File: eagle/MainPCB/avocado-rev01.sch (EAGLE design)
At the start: 163 parts, among them IC2 3V#, IC5 3V#, IC6 MCP73811/2, J1 10118194-0001LF, J2 CONNECTOR-10HEADER-5X2, J3 0475710001, J4 CONNECTOR-4HEADER4, J5 CONNECTOR-3HEADER3, J6 HR911105A, P2 CONNECTOR-15686115148922, U1 V3S, U2 AP65111A, U3 AP65111A, U4 AP65111A, U5 PMIC-LDO-XC6206P302MR(SOT23)

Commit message: in progress
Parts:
- removed C43: 10u, marius:C0603
- removed CLK, INT, RST, WOL: TEST_TESTPOINT, marius:TEST_TESTPOINT
- removed J2: CONNECTOR-10HEADER-5X2, marius:CONNECTOR-10HEADER-5X2
- added DIGITAL1, DIGITAL2, DIGITAL3, PB2, PB3: TEST_TESTPOINT, marius:TEST_TESTPOINT
- added SW1, SW2, SW3: SPST_TACT-KMR2, adafruit:SPST_TACT-KMR2
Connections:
- removed net CLK: CLK.2, J2.10
- removed net INT: INT.2, J2.9
- removed net RST: J2.3, RST.2
- removed net WOL: J2.8, WOL.2
- new net N$54: PB2.2, SW2.P, U1G$2.PB2
- new net N$57: PB3.2, U1G$2.PB3
- new net N$58: DIGITAL1.2, SW3.P, U1G$2.PG3/SDC1/D1
- new net N$61: DIGITAL2.2, SW1.P, U1G$2.PG4/SDC1/D2
- new net N$62: DIGITAL3.2, U1G$2.PG5/SDC1/D3
- net 3V3: no longer C43.1, J2.2
- net CS: no longer J2.4
- net GND: now also SW1.S, SW2.S, SW3.S; no longer C43.2, J2.1
- net MISO: no longer J2.7
- net MOSI: no longer J2.6
- net SCK: no longer J2.5

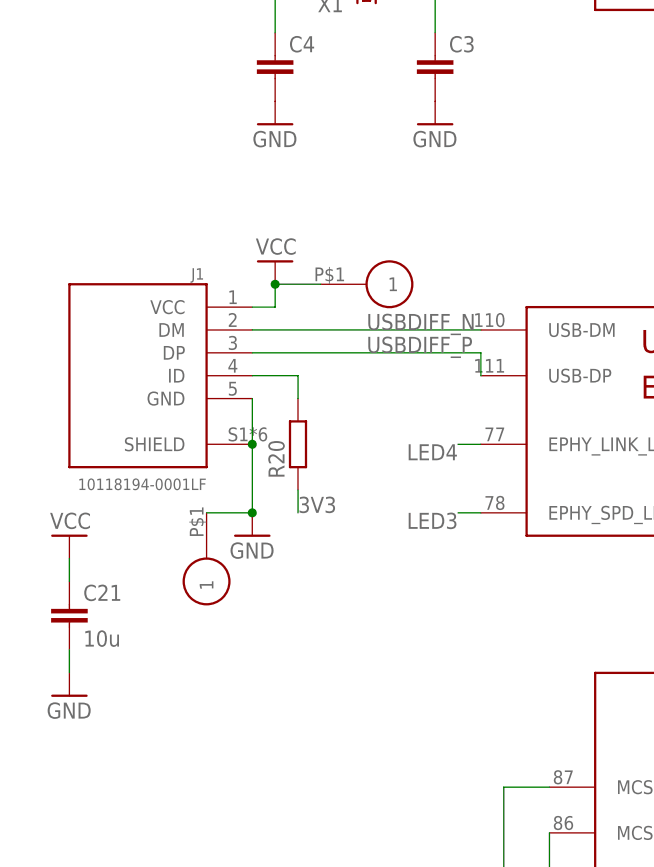
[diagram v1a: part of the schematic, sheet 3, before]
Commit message: Changed usb connector
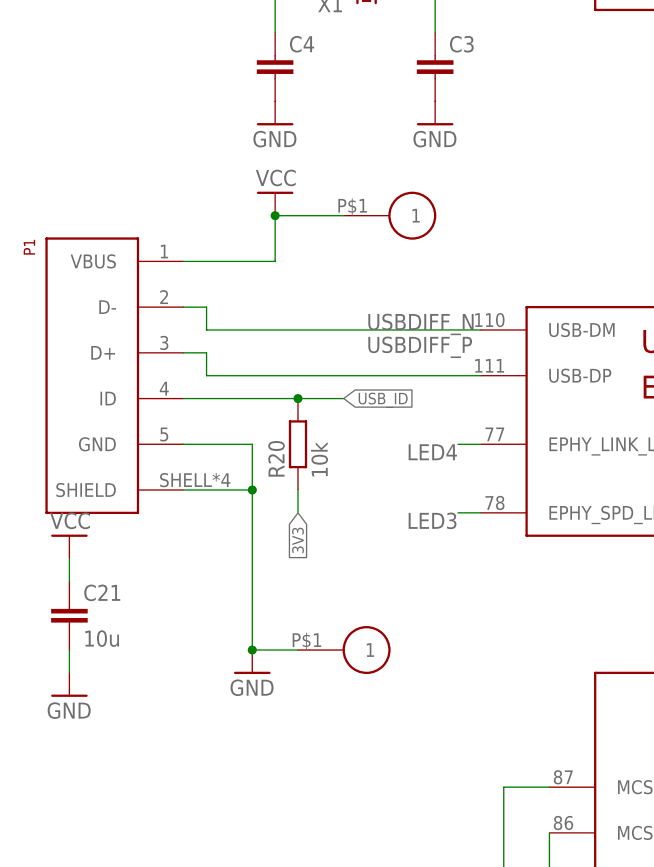
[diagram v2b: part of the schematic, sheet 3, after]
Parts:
- removed J1: 10118194-0001LF, 10118194-0001LF:10118194-0001LF
- added P1: USB629105150521, marius:USB629105150521
- R20: value (none) -> 10k
- R21, R22, R23, R24, R25, R26: device resistor:R-EU_R0402 -> marius:R0402
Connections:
- removed net USB-ID: J1.ID, R20.2
- new net USB_ID: P1.ID, R20.2, U1G$2.PF6
- net GND: now also P1.GND, P1.SHIELD; no longer J1.GND, J1.SHIELD
- net USBDIFF_N: now also P1.D-; no longer J1.DM
- net USBDIFF_P: now also P1.D+; no longer J1.DP
- net VCC: now also P1.VBUS; no longer J1.VCC

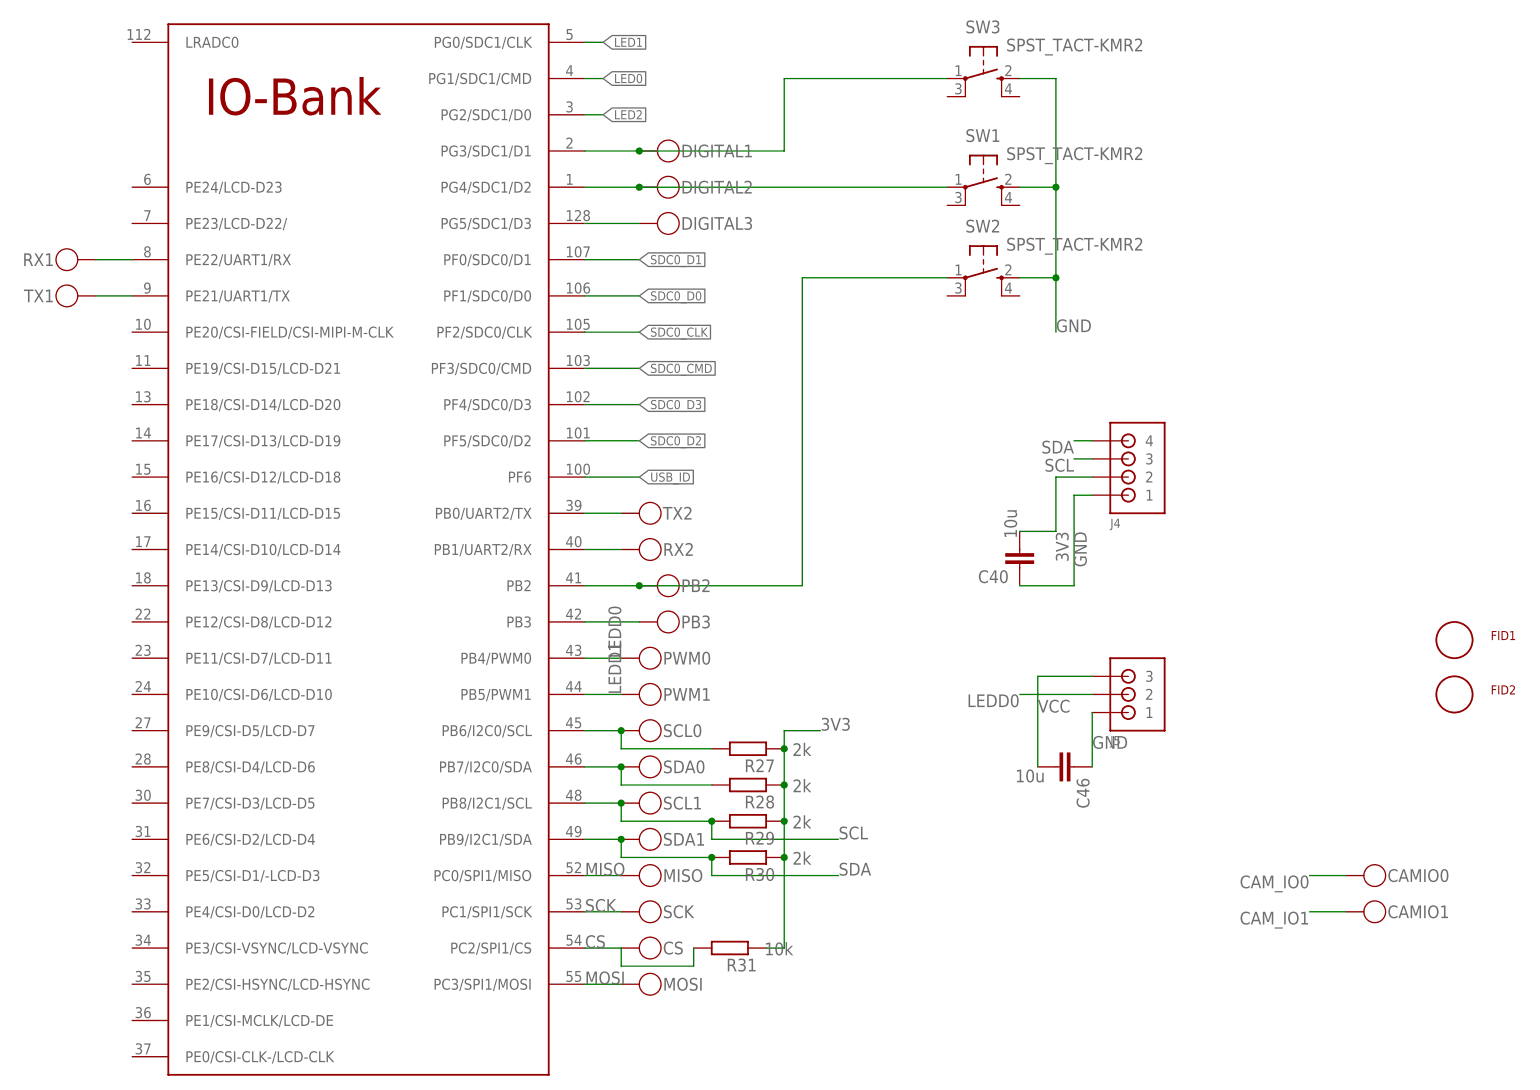
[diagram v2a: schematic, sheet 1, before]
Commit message: Added pin header for RX0/TX0
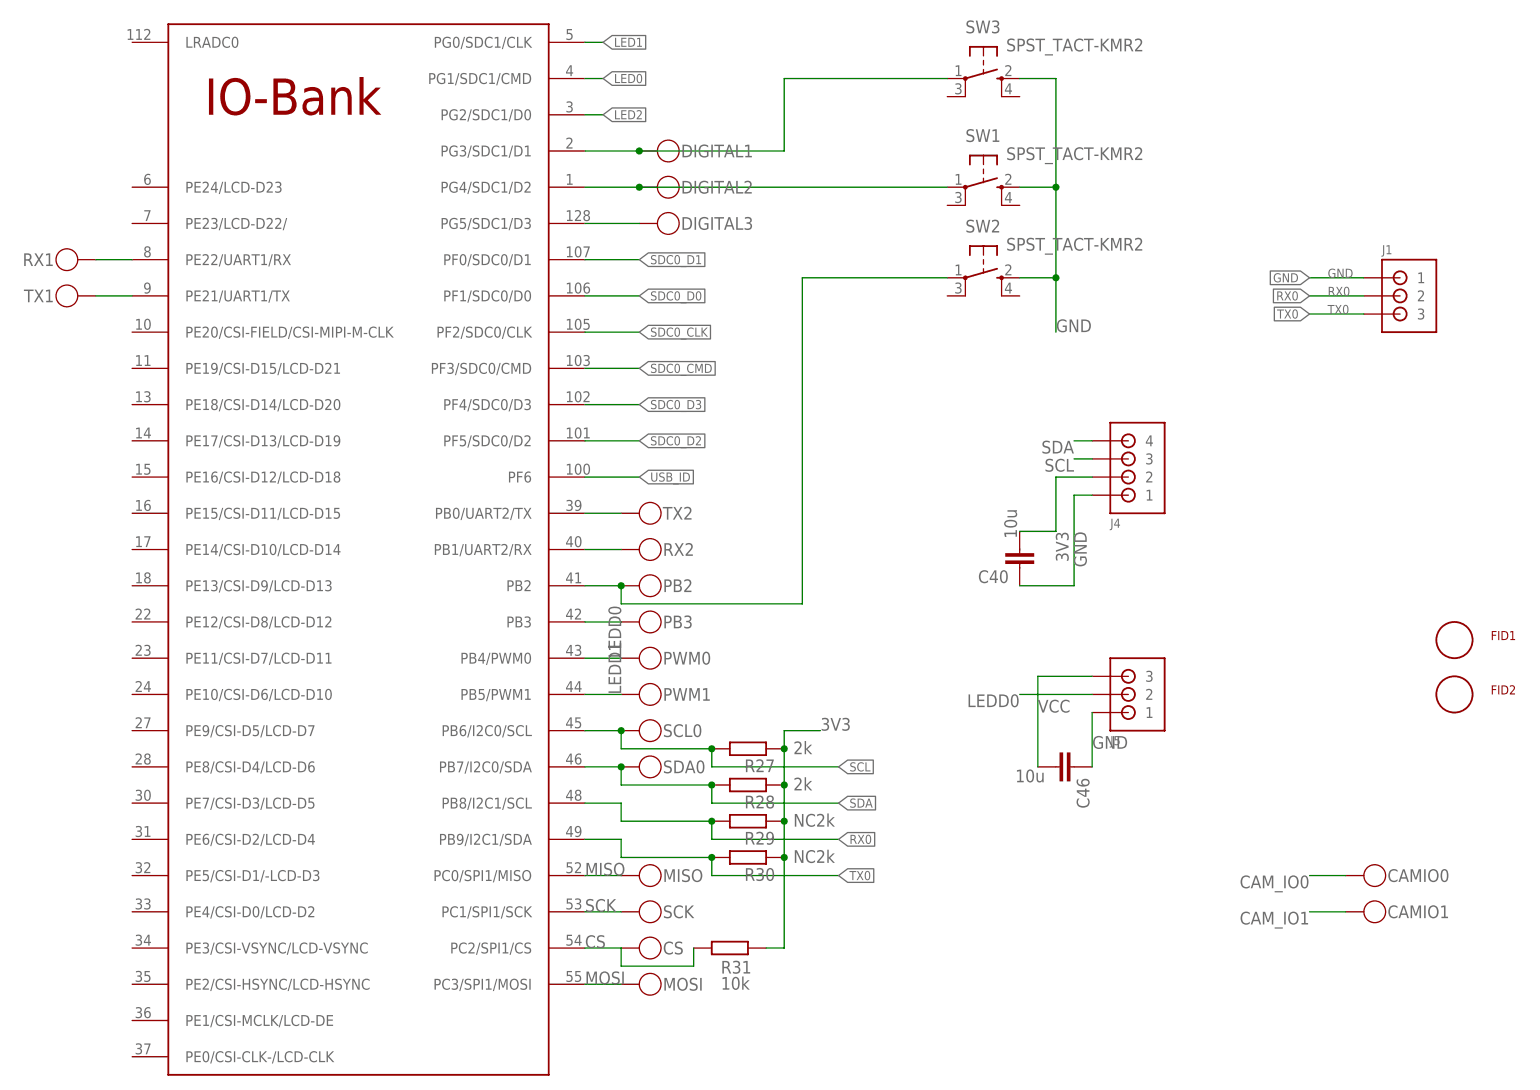
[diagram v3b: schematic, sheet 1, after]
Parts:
- removed SCL1, SDA1: TEST_TESTPOINT, marius:TEST_TESTPOINT
- added J1: CONNECTOR-3HEADER3, marius:CONNECTOR-3HEADER3
- R29, R30: value 2k -> NC2k
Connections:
- net N$47 renamed TX2
- net N$59 renamed TX1
- net N$60 renamed RX1
- removed net N$49: R27.2, SCL0.2, U1G$2.PB6/I2C0/SCL
- removed net N$50: R28.2, SDA0.2, U1G$2.PB7/I2C0/SDA
- new net RX0: J1.2, R29.2, U1G$2.PB8/I2C1/SCL
- new net TX0: J1.3, R30.2, U1G$2.PB9/I2C1/SDA
- net GND: now also J1.1
- net SCL: now also R27.2, SCL0.2, U1G$2.PB6/I2C0/SCL; no longer R29.2, SCL1.2, U1G$2.PB8/I2C1/SCL
- net SDA: now also R28.2, SDA0.2, U1G$2.PB7/I2C0/SDA; no longer R30.2, SDA1.2, U1G$2.PB9/I2C1/SDA
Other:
- moved on the sheet: PB2, PB3

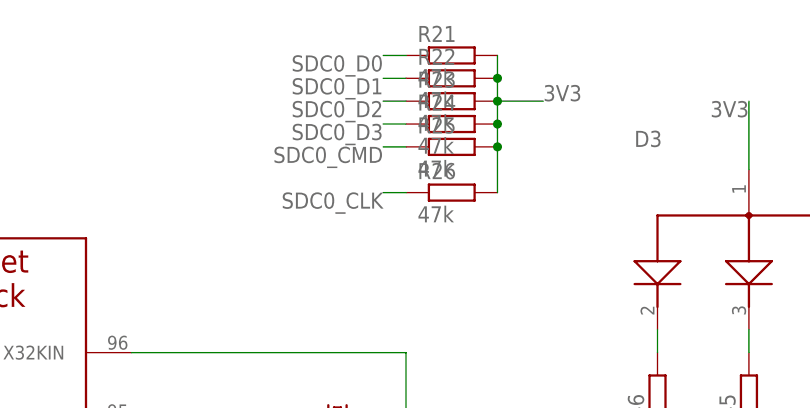
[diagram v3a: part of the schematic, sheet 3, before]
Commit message: Changed 0402 to 0603, adjusted some line
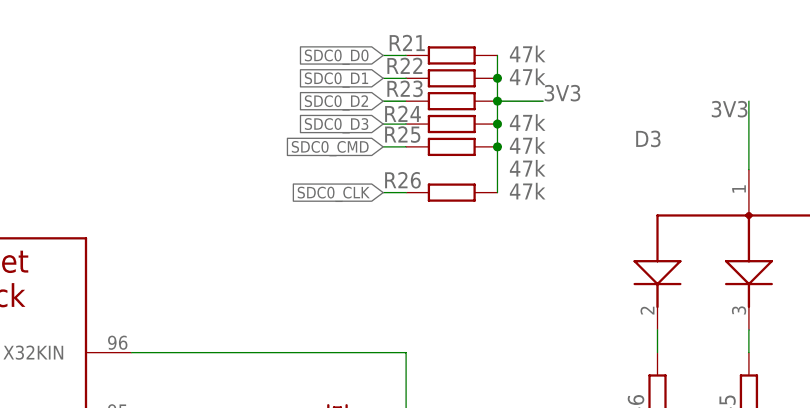
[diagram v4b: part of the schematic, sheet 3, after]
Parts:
- C1, C2, C3, C4: device marius:C0402 -> marius:C0603
- R16, R21, R22, R23, R24, R25, R26: device marius:R0402 -> marius:R0603
- renumbered 3V3 to C50
